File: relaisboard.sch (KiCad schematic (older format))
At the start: 7 parts

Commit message: Odroid
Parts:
- added 47k: R, symbol R
- added S? (x2): dip, symbol dip
- added U?: ULN2003A, symbol ULN2003A
- added U?: PCF8574, symbol PCF8574
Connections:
- net A2 is gone; now on net VCC: K?.1
- net A3 is gone; now on net VCC: K?.1
- net A4 is gone; now on net VCC: K?.1
- net A5 is gone; now on net VCC: K?.1
- net A6 is gone; now on net VCC: K?.1
- net A7 is gone; now on net VCC: K?.1
- net GND: now also S?.~, U?.8 (GND), U?.8 (VSS), U?.9 (COM); no longer K?.2, K?.2, K?.2, K?.2, K?.2, K?.2, K?.2
- net A1 renamed VCC
- net VCC: now also 47k.2, U?.16 (VDD)
- new net: K?.2, U?.16 (O1)
- new net: K?.2, U?.15 (O2)
- new net: K?.2, U?.14 (O3)
- new net: K?.2, U?.13 (O4)
- new net: K?.2, U?.12 (O5)
- new net: K?.2, U?.11 (O6)
- new net: K?.2, U?.10 (O7)
- new net: U?.1 (I1), U?.4 (P0)
- new net: U?.2 (I2), U?.5 (P1)
- new net: U?.3 (I3), U?.6 (P2)
- new net: U?.4 (I4), U?.7 (P3)
- new net: U?.5 (I5), U?.9 (P4)
- new net: U?.10 (P5), U?.6 (I6)
- new net: U?.11 (P6), U?.7 (I7)
- new net: S?.~, S?.~, U?.1 (A0)
- new net: S?.~, S?.~, U?.2 (A1)
- new net: S?.~, S?.~, U?.3 (A2)
- new net: 47k.1, S?.~
- new net SCL: U?.14 (SCL)
- new net SDA: U?.15 (SDA)
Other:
- moved on the sheet: K?

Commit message: no idea what to write.
something :-D
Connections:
- net at S?.~: now also 47k.1
- new net: S?.~, S?.~, U?.1 (A0)
- new net: S?.~, S?.~, U?.2 (A1)
- new net: S?.~, S?.~, U?.3 (A2)
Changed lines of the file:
@@
 $Descr A4 11693 8268
 encoding utf-8
-Sheet 4 7
+Sheet 4 8
 Title ""
 Date ""

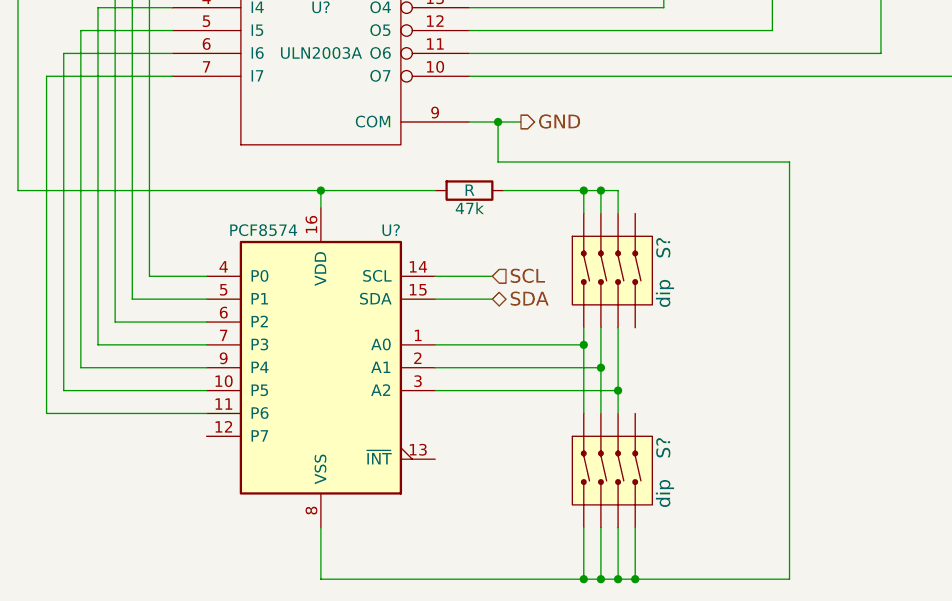
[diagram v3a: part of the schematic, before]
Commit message: added teensy library
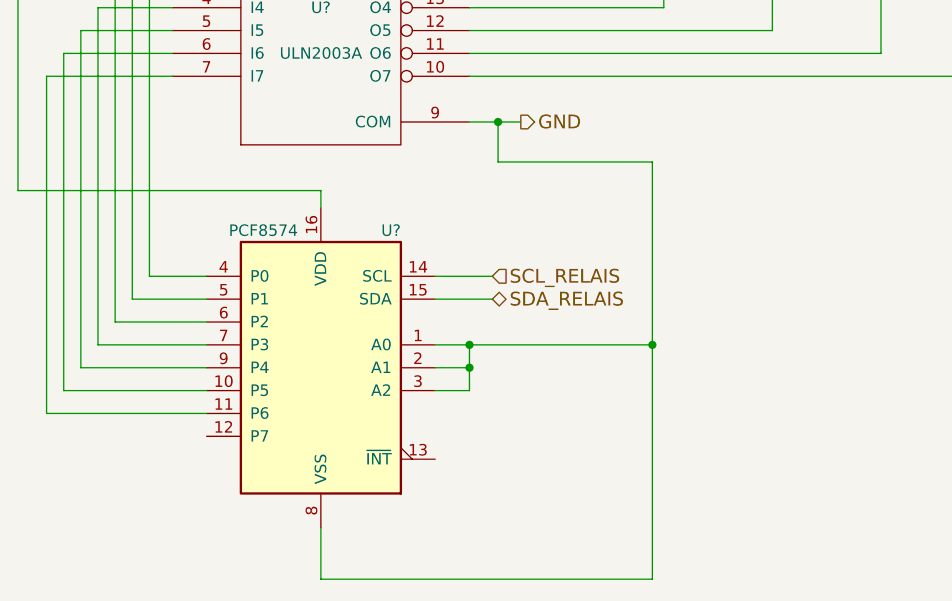
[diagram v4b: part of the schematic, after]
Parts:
- removed 47k: R, symbol R
- removed S? (x2): dip, symbol dip
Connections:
- net GND: now also U?.1 (A0), U?.2 (A1), U?.3 (A2)
- net SCL renamed SCL_RELAIS
- net SDA renamed SDA_RELAIS
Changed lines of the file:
@@
 LIBS:valves
 LIBS:selfmade
+LIBS:teensy
 LIBS:preamp-cache
 EELAYER 25 0
@@
 	4000 4625 4000 4550
 Wire Wire Line
-	2675 4550 4500 4550
+	4000 4550 2675 4550
 Wire Wire Line
 	2675 4550 2675 2450
@@
 	4000 6025 4000 6250
 Wire Wire Line
-	4000 6250 6050 6250
-Wire Wire Line
-	6050 6250 6050 4425
-Wire Wire Line
-	6050 4425 4775 4425
+	4000 6250 5450 6250
+Wire Wire Line
+	5450 6250 5450 4425
+Wire Wire Line
+	5450 4425 4775 4425
 Wire Wire Line
 	4775 4425 4775 4250
 Connection ~ 4775 4250
 Text HLabel 4750 4925 2    60   Input ~ 0
-SCL
+SCL_RELAIS
 Text HLabel 4750 5025 2    60   BiDi ~ 0
-SDA
+SDA_RELAIS
 Wire Wire Line
 	4750 4925 4500 4925
 Wire Wire Line
 	4500 5025 4750 5025
-$Comp
-L dip S?
-U 1 1 588BD9E4
-P 5100 5625
-F 0 "S?" H 5150 6025 60  0000 C CNN
-F 1 "dip" H 5350 6025 60  0000 C CNN
-F 2 "" H 5100 5625 60  0001 C CNN
-F 3 "" H 5100 5625 60  0001 C CNN
-	1    5100 5625
-	0    1    1    0
-$EndComp
-$Comp
-L dip S?
-U 1 1 588BDA67
-P 5100 4750
-F 0 "S?" H 5150 5150 60  0000 C CNN
-F 1 "dip" H 5350 5150 60  0000 C CNN
-F 2 "" H 5100 4750 60  0001 C CNN
-F 3 "" H 5100 4750 60  0001 C CNN
-	1    5100 4750
-	0    1    1    0
-$EndComp
-Wire Wire Line
-	5150 6025 5150 6250
-Connection ~ 5150 6250
-Wire Wire Line
-	5225 6025 5225 6250
-Connection ~ 5225 6250
-Wire Wire Line
-	5300 6025 5300 6250
-Connection ~ 5300 6250
-Wire Wire Line
-	5375 6025 5375 6250
-Connection ~ 5375 6250
-Wire Wire Line
-	4500 5225 5150 5225
-Wire Wire Line
-	5150 5150 5150 5525
-Wire Wire Line
-	4500 5325 5225 5325
-Wire Wire Line
-	5225 5150 5225 5525
-Wire Wire Line
-	4500 5425 5300 5425
-Wire Wire Line
-	5300 5150 5300 5525
-Connection ~ 5150 5225
-Connection ~ 5225 5325
-Connection ~ 5300 5425
-$Comp
-L R 47k
-U 1 1 588BE1C4
-P 4650 4550
-F 0 "47k" V 4730 4550 50  0000 C CNN
-F 1 "R" V 4650 4550 50  0000 C CNN
-F 2 "" V 4580 4550 50  0000 C CNN
-F 3 "" H 4650 4550 50  0000 C CNN
-	1    4650 4550
-	0    1    1    0
-$EndComp
-Connection ~ 4000 4550
-Wire Wire Line
-	4800 4550 5300 4550
-Wire Wire Line
-	5150 4550 5150 4650
-Wire Wire Line
-	5225 4550 5225 4650
-Connection ~ 5150 4550
-Wire Wire Line
-	5300 4550 5300 4650
-Connection ~ 5225 4550
+Wire Wire Line
+	4500 5225 5450 5225
+Connection ~ 5450 5225
+Wire Wire Line
+	4500 5325 4650 5325
+Wire Wire Line
+	4650 5225 4650 5425
+Connection ~ 4650 5225
+Wire Wire Line
+	4650 5425 4500 5425
+Connection ~ 4650 5325
 $EndSCHEMATC

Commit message: Weiterentwicklung des Netzteiles
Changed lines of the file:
@@
 $Descr A4 11693 8268
 encoding utf-8
-Sheet 4 8
+Sheet 2 12
 Title ""
 Date ""
@@
 Text HLabel 3150 1250 0    60   Input ~ 0
 L_I
-Text HLabel 3150 1325 0    60   Output ~ 0
-PE_I
 Text HLabel 3150 1400 0    60   Output ~ 0
 N_I
@@
 	4125 1525 4125 1250
 Wire Wire Line
-	4125 1250 6725 1250
-Wire Wire Line
-	3150 1325 7275 1325
+	4125 1250 4825 1250
+Wire Wire Line
+	4825 1250 5300 1250
+Wire Wire Line
+	5300 1250 5775 1250
+Wire Wire Line
+	5775 1250 6250 1250
+Wire Wire Line
+	6250 1250 6725 1250
 Wire Wire Line
 	4825 1250 4825 1825
@@
 Wire Wire Line
 	6925 1775 7275 1775
-Text HLabel 7275 1325 2    60   Input ~ 0
-PE_O
 Text HLabel 7275 1400 2    60   Input ~ 0
 N_O
@@
 U 1 1 5883A32A
 P 3525 1825
+AR Path="/58B9DD1B/58BA9A19/5883A32A" Ref="K?"  Part="1"
+AR Path="/58838AD0/5883A32A" Ref="K?"  Part="1"
 F 0 "K?" H 3325 2025 50  0000 L CNN
 F 1 "OPTO_TRIAC" H 3325 1625 50  0000 L CNN
@@
 U 1 1 5883A37E
 P 4025 1825
+AR Path="/58B9DD1B/58BA9A19/5883A37E" Ref="K?"  Part="1"
+AR Path="/58838AD0/5883A37E" Ref="K?"  Part="1"
 F 0 "K?" H 3825 2025 50  0000 L CNN
 F 1 "OPTO_TRIAC" H 3825 1625 50  0000 L CNN
@@
 U 1 1 5883A3AA
 P 4925 2125
+AR Path="/58B9DD1B/58BA9A19/5883A3AA" Ref="K?"  Part="1"
+AR Path="/58838AD0/5883A3AA" Ref="K?"  Part="1"
 F 0 "K?" H 4725 2325 50  0000 L CNN
 F 1 "OPTO_TRIAC" H 4725 1925 50  0000 L CNN
@@
 U 1 1 5883A3D7
 P 5400 2125
+AR Path="/58B9DD1B/58BA9A19/5883A3D7" Ref="K?"  Part="1"
+AR Path="/58838AD0/5883A3D7" Ref="K?"  Part="1"
 F 0 "K?" H 5200 2325 50  0000 L CNN
 F 1 "OPTO_TRIAC" H 5200 1925 50  0000 L CNN
@@
 U 1 1 5883A40D
 P 5875 2125
+AR Path="/58B9DD1B/58BA9A19/5883A40D" Ref="K?"  Part="1"
+AR Path="/58838AD0/5883A40D" Ref="K?"  Part="1"
 F 0 "K?" H 5675 2325 50  0000 L CNN
 F 1 "OPTO_TRIAC" H 5675 1925 50  0000 L CNN
@@
 U 1 1 5883A442
 P 6350 2125
+AR Path="/58B9DD1B/58BA9A19/5883A442" Ref="K?"  Part="1"
+AR Path="/58838AD0/5883A442" Ref="K?"  Part="1"
 F 0 "K?" H 6150 2325 50  0000 L CNN
 F 1 "OPTO_TRIAC" H 6150 1925 50  0000 L CNN
@@
 U 1 1 5883A474
 P 6825 2125
+AR Path="/58B9DD1B/58BA9A19/5883A474" Ref="K?"  Part="1"
+AR Path="/58838AD0/5883A474" Ref="K?"  Part="1"
 F 0 "K?" H 6625 2325 50  0000 L CNN
 F 1 "OPTO_TRIAC" H 6625 1925 50  0000 L CNN
@@
 U 1 1 588A735C
 P 4000 3850
+AR Path="/58B9DD1B/58BA9A19/588A735C" Ref="U?"  Part="1"
+AR Path="/58838AD0/588A735C" Ref="U?"  Part="1"
 F 0 "U?" H 4000 3950 50  0000 C CNN
 F 1 "ULN2003A" H 4000 3750 50  0000 C CNN
@@
 VCC
 Wire Wire Line
-	3150 2600 6725 2600
+	3150 2600 3300 2600
+Wire Wire Line
+	3300 2600 3425 2600
+Wire Wire Line
+	3425 2600 3925 2600
+Wire Wire Line
+	3925 2600 4825 2600
+Wire Wire Line
+	4825 2600 5300 2600
+Wire Wire Line
+	5300 2600 5775 2600
+Wire Wire Line
+	5775 2600 6250 2600
+Wire Wire Line
+	6250 2600 6725 2600
 Wire Wire Line
 	3425 2600 3425 2125
@@
 U 1 1 588A816E
 P 4000 5325
+AR Path="/58B9DD1B/58BA9A19/588A816E" Ref="U?"  Part="1"
+AR Path="/58838AD0/588A816E" Ref="U?"  Part="1"
 F 0 "U?" H 3650 5925 50  0000 L CNN
 F 1 "PCF8574" H 4100 5925 50  0000 L CNN
@@
 	2800 4050 3350 4050
 Wire Wire Line
-	4650 4250 4875 4250
+	4650 4250 4775 4250
+Wire Wire Line
+	4775 4250 4875 4250
 Wire Wire Line
 	4000 6025 4000 6250
@@
 	4000 6250 5450 6250
 Wire Wire Line
-	5450 6250 5450 4425
+	5450 6250 5450 5225
+Wire Wire Line
+	5450 5225 5450 4425
 Wire Wire Line
 	5450 4425 4775 4425
@@
 	4500 5025 4750 5025
 Wire Wire Line
-	4500 5225 5450 5225
+	4500 5225 4650 5225
+Wire Wire Line
+	4650 5225 5450 5225
 Connection ~ 5450 5225
 Wire Wire Line
 	4500 5325 4650 5325
 Wire Wire Line
-	4650 5225 4650 5425
+	4650 5225 4650 5325
+Wire Wire Line
+	4650 5325 4650 5425
 Connection ~ 4650 5225
 Wire Wire Line
